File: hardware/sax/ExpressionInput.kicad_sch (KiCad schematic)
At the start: 5 parts

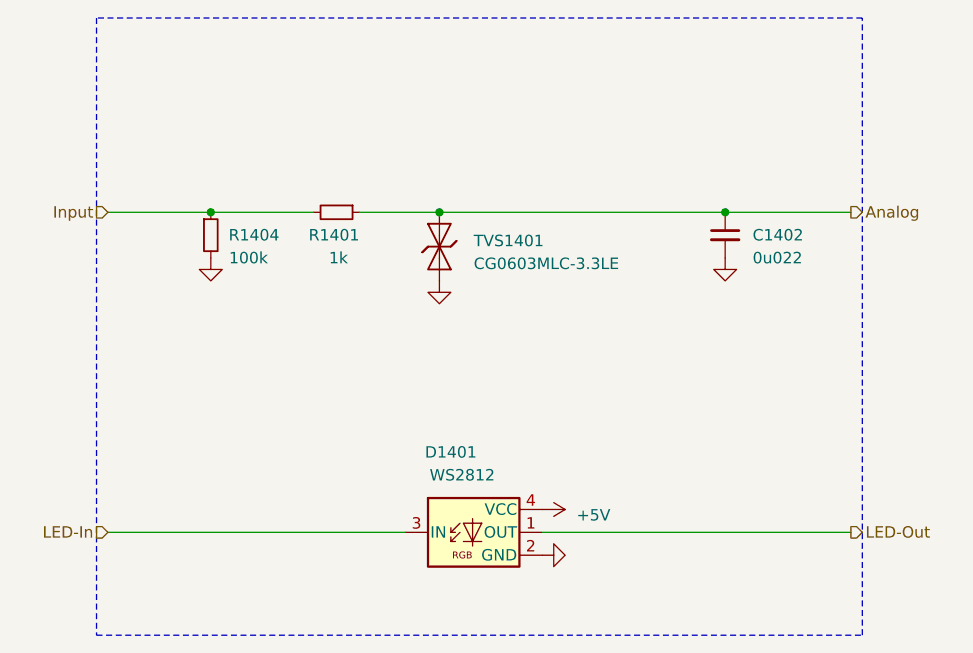
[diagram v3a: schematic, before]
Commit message: sax2 -> sax
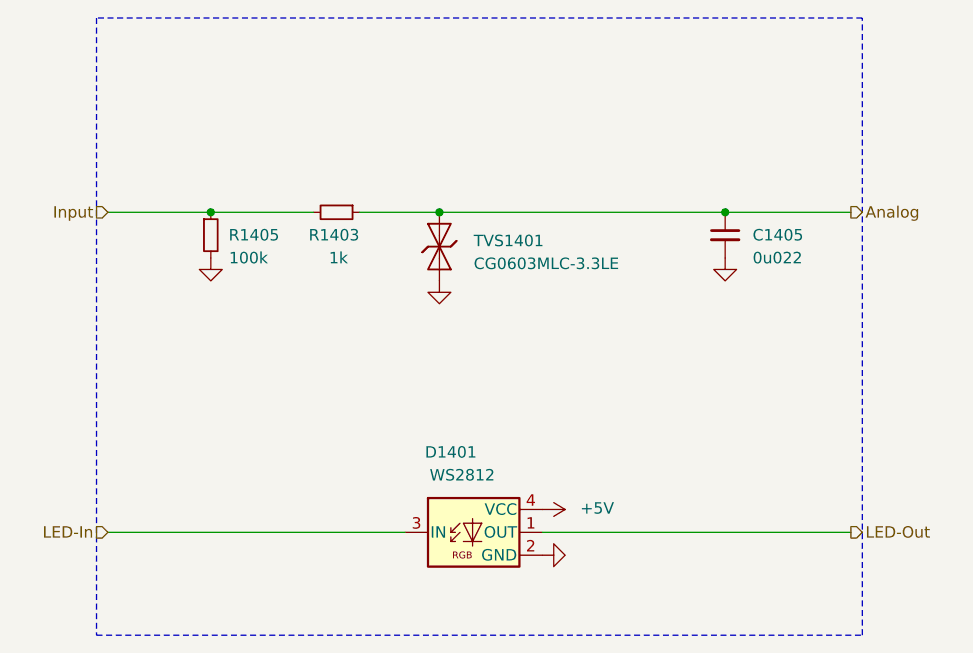
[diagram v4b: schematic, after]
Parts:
- renumbered C1402 to C1405, R1401 to R1403, R1404 to R1405
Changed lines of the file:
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@@
 		(on_board yes)
 		(dnp no)
-		(property "Reference" "R1401"
+		(property "Reference" "R1403"
 			(at 139.7001 95.25 90)
 			(effects
@@
 		)
 		(instances
-			(project "sax"
+			(project "sax2"
 				(path "/6c8448b4-b04d-47e1-934e-e40cbe27a7be/986c2710-b6fb-48af-9291-0e7dc7b5abf9/09fde53a-0726-4a1a-ba32-997a9c8cb2ac"
 					(reference "R1701")
@@
 				)
 				(path "/6c8448b4-b04d-47e1-934e-e40cbe27a7be/986c2710-b6fb-48af-9291-0e7dc7b5abf9/75bdefb6-cbec-430c-b2f6-bba8982a1e16"
-					(reference "R1401")
+					(reference "R1403")
 					(unit 1)
 				)
@@
 		(dnp no)
 		(fields_autoplaced yes)
-		(property "Reference" "#PWR1404"
+		(property "Reference" "#PWR1414"
 			(at 123.19 104.14 0)
 			(effects
@@
 		)
 		(instances
-			(project "sax"
+			(project "sax2"
 				(path "/6c8448b4-b04d-47e1-934e-e40cbe27a7be/986c2710-b6fb-48af-9291-0e7dc7b5abf9/09fde53a-0726-4a1a-ba32-997a9c8cb2ac"
 					(reference "#PWR1701")
@@
 				)
 				(path "/6c8448b4-b04d-47e1-934e-e40cbe27a7be/986c2710-b6fb-48af-9291-0e7dc7b5abf9/75bdefb6-cbec-430c-b2f6-bba8982a1e16"
-					(reference "#PWR1404")
+					(reference "#PWR1414")
 					(unit 1)
 				)
@@
 		(on_board yes)
 		(dnp no)
-		(fields_autoplaced yes)
-		(property "Reference" "#PWR1417"
+		(property "Reference" "#PWR1423"
 			(at 156.21 125.73 0)
 			(effects
@@
 		)
 		(property "Value" "+5V"
-			(at 163.83 126.365 90)
-			(effects
-				(font
-					(size 1.27 1.27)
-				)
-				(justify left)
+			(at 166.116 125.603 90)
+			(effects
+				(font
+					(size 1.27 1.27)
+					(color 255 92 187 1)
+				)
 			)
 		)
@@
 		)
 		(instances
-			(project "sax"
+			(project "sax2"
 				(path "/6c8448b4-b04d-47e1-934e-e40cbe27a7be/986c2710-b6fb-48af-9291-0e7dc7b5abf9/09fde53a-0726-4a1a-ba32-997a9c8cb2ac"
 					(reference "#PWR1704")
@@
 				)
 				(path "/6c8448b4-b04d-47e1-934e-e40cbe27a7be/986c2710-b6fb-48af-9291-0e7dc7b5abf9/75bdefb6-cbec-430c-b2f6-bba8982a1e16"
-					(reference "#PWR1417")
+					(reference "#PWR1423")
 					(unit 1)
 				)
@@
 		(dnp no)
 		(fields_autoplaced yes)
-		(property "Reference" "#PWR1405"
+		(property "Reference" "#PWR1416"
 			(at 180.34 104.14 0)
 			(effects
@@
 		)
 		(instances
-			(project "sax"
+			(project "sax2"
 				(path "/6c8448b4-b04d-47e1-934e-e40cbe27a7be/986c2710-b6fb-48af-9291-0e7dc7b5abf9/09fde53a-0726-4a1a-ba32-997a9c8cb2ac"
 					(reference "#PWR1702")
@@
 				)
 				(path "/6c8448b4-b04d-47e1-934e-e40cbe27a7be/986c2710-b6fb-48af-9291-0e7dc7b5abf9/75bdefb6-cbec-430c-b2f6-bba8982a1e16"
-					(reference "#PWR1405")
+					(reference "#PWR1416")
 					(unit 1)
 				)
@@
 		(on_board yes)
 		(dnp no)
-		(property "Reference" "C1402"
+		(property "Reference" "C1405"
 			(at 183.388 95.25 0)
 			(effects
@@
 		)
 		(instances
-			(project "sax"
+			(project "sax2"
 				(path "/6c8448b4-b04d-47e1-934e-e40cbe27a7be/986c2710-b6fb-48af-9291-0e7dc7b5abf9/09fde53a-0726-4a1a-ba32-997a9c8cb2ac"
 					(reference "C1701")
@@
 				)
 				(path "/6c8448b4-b04d-47e1-934e-e40cbe27a7be/986c2710-b6fb-48af-9291-0e7dc7b5abf9/75bdefb6-cbec-430c-b2f6-bba8982a1e16"
-					(reference "C1402")
+					(reference "C1405")
 					(unit 1)
 				)
@@
 		)
 		(instances
-			(project "sax"
+			(project "sax2"
 				(path "/6c8448b4-b04d-47e1-934e-e40cbe27a7be/986c2710-b6fb-48af-9291-0e7dc7b5abf9/09fde53a-0726-4a1a-ba32-997a9c8cb2ac"
 					(reference "TVS1701")
@@
 		(dnp no)
 		(fields_autoplaced yes)
-		(property "Reference" "#PWR1418"
+		(property "Reference" "#PWR1425"
 			(at 166.37 130.81 0)
 			(effects
@@
 		)
 		(instances
-			(project "sax"
+			(project "sax2"
 				(path "/6c8448b4-b04d-47e1-934e-e40cbe27a7be/986c2710-b6fb-48af-9291-0e7dc7b5abf9/09fde53a-0726-4a1a-ba32-997a9c8cb2ac"
 					(reference "#PWR1705")
@@
 				)
 				(path "/6c8448b4-b04d-47e1-934e-e40cbe27a7be/986c2710-b6fb-48af-9291-0e7dc7b5abf9/75bdefb6-cbec-430c-b2f6-bba8982a1e16"
-					(reference "#PWR1418")
+					(reference "#PWR1425")
 					(unit 1)
 				)
@@
 		(dnp no)
 		(fields_autoplaced yes)
-		(property "Reference" "#PWR1407"
+		(property "Reference" "#PWR1418"
 			(at 148.59 106.68 0)
 			(effects
@@
 		)
 		(instances
-			(project "sax"
+			(project "sax2"
 				(path "/6c8448b4-b04d-47e1-934e-e40cbe27a7be/986c2710-b6fb-48af-9291-0e7dc7b5abf9/09fde53a-0726-4a1a-ba32-997a9c8cb2ac"
 					(reference "#PWR1703")
@@
 				)
 				(path "/6c8448b4-b04d-47e1-934e-e40cbe27a7be/986c2710-b6fb-48af-9291-0e7dc7b5abf9/75bdefb6-cbec-430c-b2f6-bba8982a1e16"
-					(reference "#PWR1407")
+					(reference "#PWR1418")
 					(unit 1)
 				)
@@
 		)
 		(instances
-			(project "sax"
+			(project "sax2"
 				(path "/6c8448b4-b04d-47e1-934e-e40cbe27a7be/986c2710-b6fb-48af-9291-0e7dc7b5abf9/09fde53a-0726-4a1a-ba32-997a9c8cb2ac"
 					(reference "D1701")
@@
 		(on_board yes)
 		(dnp no)
-		(property "Reference" "R1404"
+		(property "Reference" "R1405"
 			(at 130.81 95.2499 0)
 			(effects
@@
 		)
 		(instances
-			(project "sax"
+			(project "sax2"
 				(path "/6c8448b4-b04d-47e1-934e-e40cbe27a7be/986c2710-b6fb-48af-9291-0e7dc7b5abf9/09fde53a-0726-4a1a-ba32-997a9c8cb2ac"
 					(reference "R1702")
@@
 				)
 				(path "/6c8448b4-b04d-47e1-934e-e40cbe27a7be/986c2710-b6fb-48af-9291-0e7dc7b5abf9/75bdefb6-cbec-430c-b2f6-bba8982a1e16"
-					(reference "R1404")
-					(unit 1)
-				)
+					(reference "R1405")
+					(unit 1)
+				)

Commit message: Replace step-down
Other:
- title: Expression Input -> V2 sax
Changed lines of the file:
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@@
 	(paper "A4")
 	(title_block
-		(title "Expression Input")
-		(date "2026-03-21")
-		(rev "2026-02-10")
+		(title "V2 sax")
+		(date "2026-03-31")
+		(rev "2026-03-31")
 		(company "Versio Duo")
 	)
